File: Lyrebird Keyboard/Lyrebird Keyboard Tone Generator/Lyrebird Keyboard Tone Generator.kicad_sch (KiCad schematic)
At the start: 111 parts, among them J1 Edge Connector, J10 C# 4434 Hz, J11 G# 6642 Hz, J12 D 4697 Hz, J13 F# 5923 Hz, J2 A 3520 Hz, J3 D# 4976 Hz, J4 A# 3726 Hz, J5 E 5274 Hz, J6 B 3949 Hz, J7 F 5590 Hz, J8 C 4188 Hz, J9 G 6275 Hz, U1 LM358, U10 LM358, U11 LM358, U12 LM358, U13 4069, U14 4069, U2 LM358, U3 LM358, U4 LM358, U5 LM358, U6 LM358, U7 LM358, U8 LM358, U9 LM358

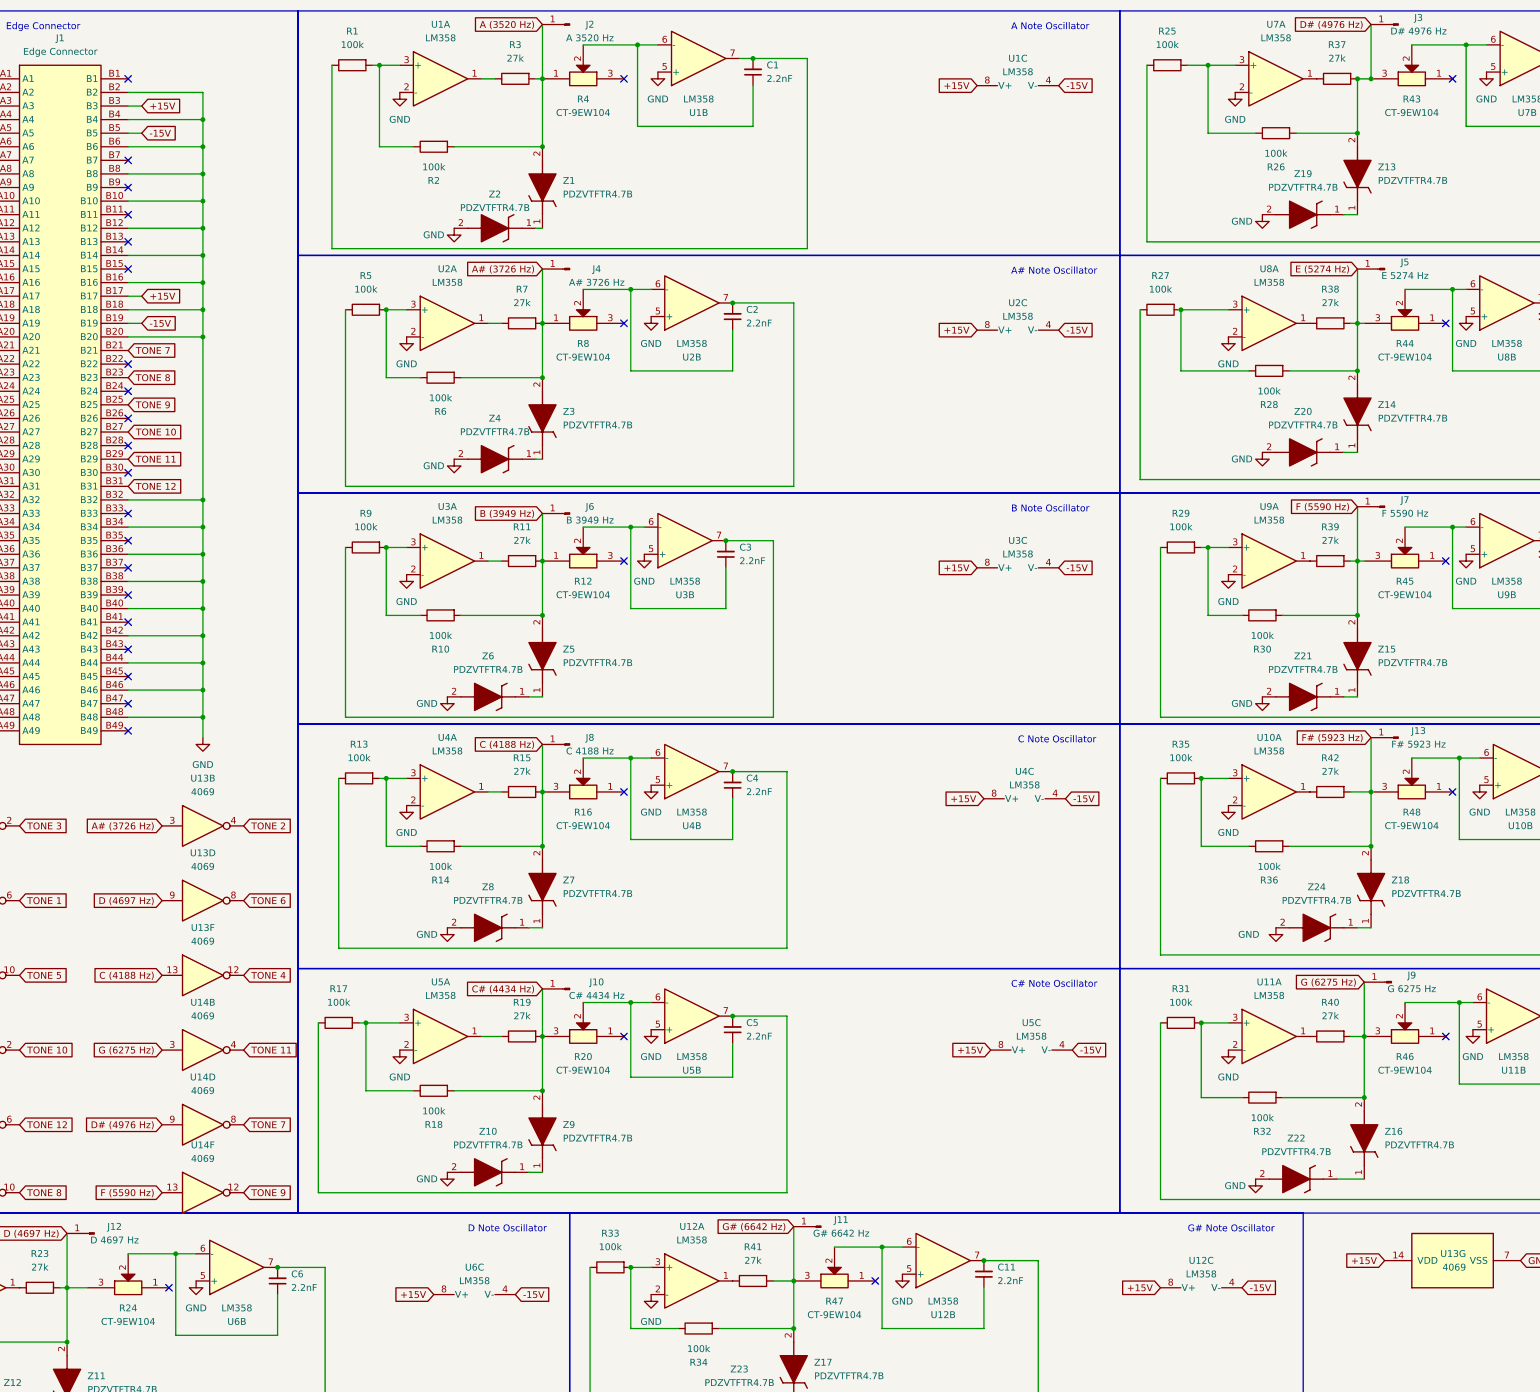
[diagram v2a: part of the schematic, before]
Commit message: Move PSU and Amp off of mainboard
Moved Power Supply to its own board, single layer.  Moved Class D amp onto a daughter board, modifiying to also have a 1/4" balanced output as well as amplified output
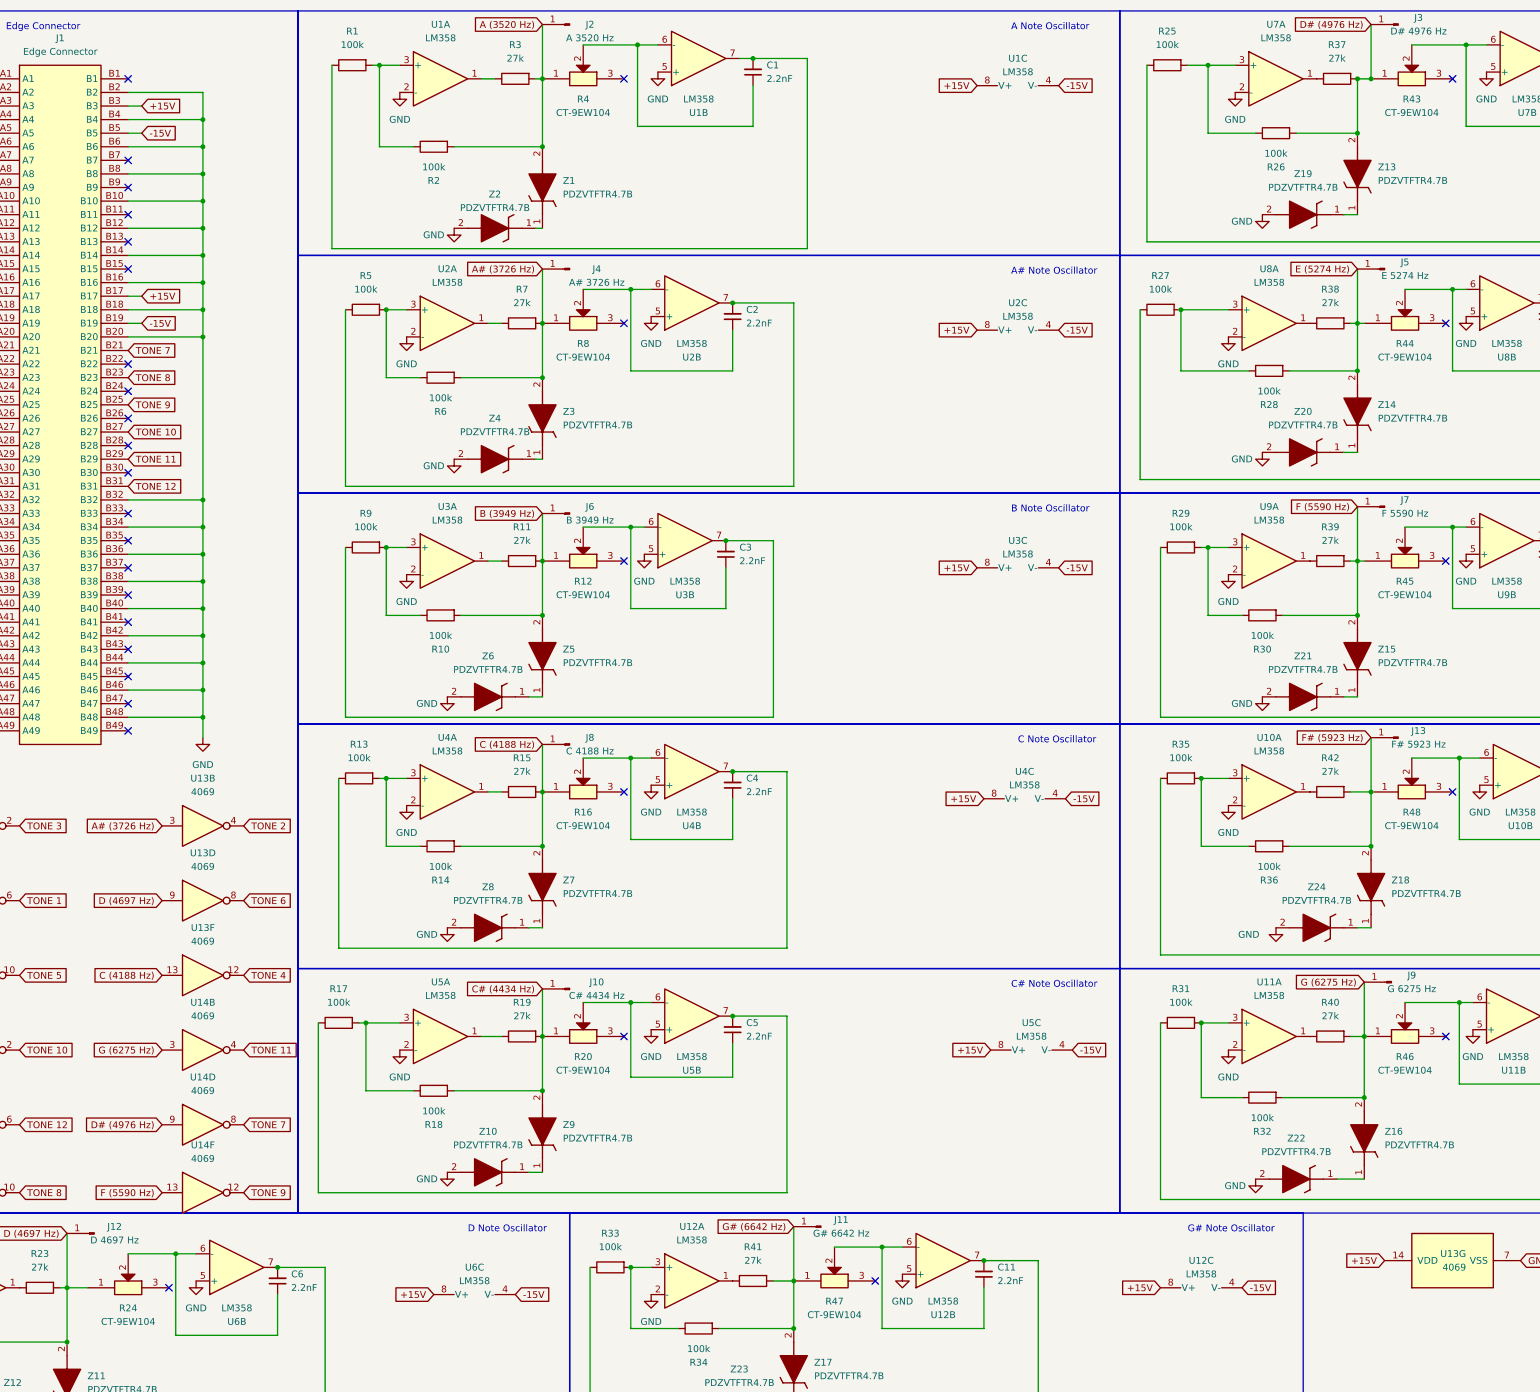
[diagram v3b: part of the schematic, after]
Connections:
- net C (4188 Hz): now also R16.1; no longer R16.3
- net C# (4434 Hz): now also R20.1; no longer R20.3
- net D (4697 Hz): now also R24.1; no longer R24.3
- net D# (4976 Hz): now also R43.1; no longer R43.3
- net E (5274 Hz): now also R44.1; no longer R44.3
- net F (5590 Hz): now also R45.1; no longer R45.3
- net F# (5923 Hz): now also R48.1; no longer R48.3
- net G (6275 Hz): now also R46.1; no longer R46.3
- net G# (6642 Hz): now also R47.1; no longer R47.3
